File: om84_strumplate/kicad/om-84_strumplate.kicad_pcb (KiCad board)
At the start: 2 copper layers, 117.2 x 151.8 mm, 0 parts

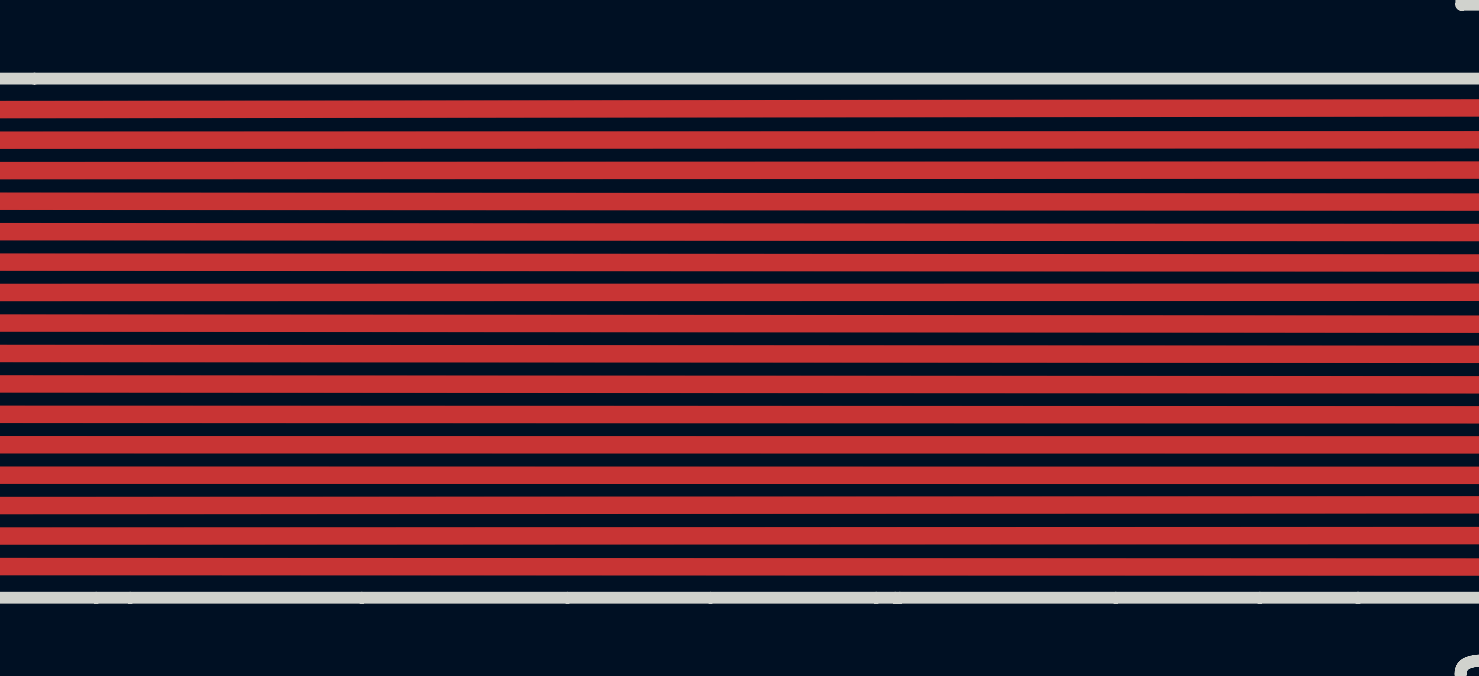
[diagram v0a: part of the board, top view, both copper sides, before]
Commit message: Add Key & Cable Co. branding to both flex tails
White silkscreen on the ribbon tail of the OM-84 and OM-27 flex PCBs:
the piano-key mark (10 mm, white key outlined, black key and plug
filled, cable as a 0.25 mm stroke), "Key & Cable Co." and
"keyandcable.com" in stroke text, and a QR code for
https://keyandcable.com. The QR is version 3 at ECC level H; the ink
prints the light modules and a 3-module quiet zone so the amber
coverlay forms the dark modules. OM-84 uses 0.45 mm modules, the
narrower OM-27 tail uses 0.42 mm. Everything sits over the traces,
clear of the contacts, mask openings and gold-finger stiffeners.

The artwork lives in lib/keyandcable_branding.pretty as reusable
footprints, with a project fp-lib-table in each KiCad folder.
F_Silkscreen gerbers re-plotted with the stored board plot settings
and the production zips updated.

Co-Authored-By: Claude Fable 5.1 <noreply@anthropic.com>
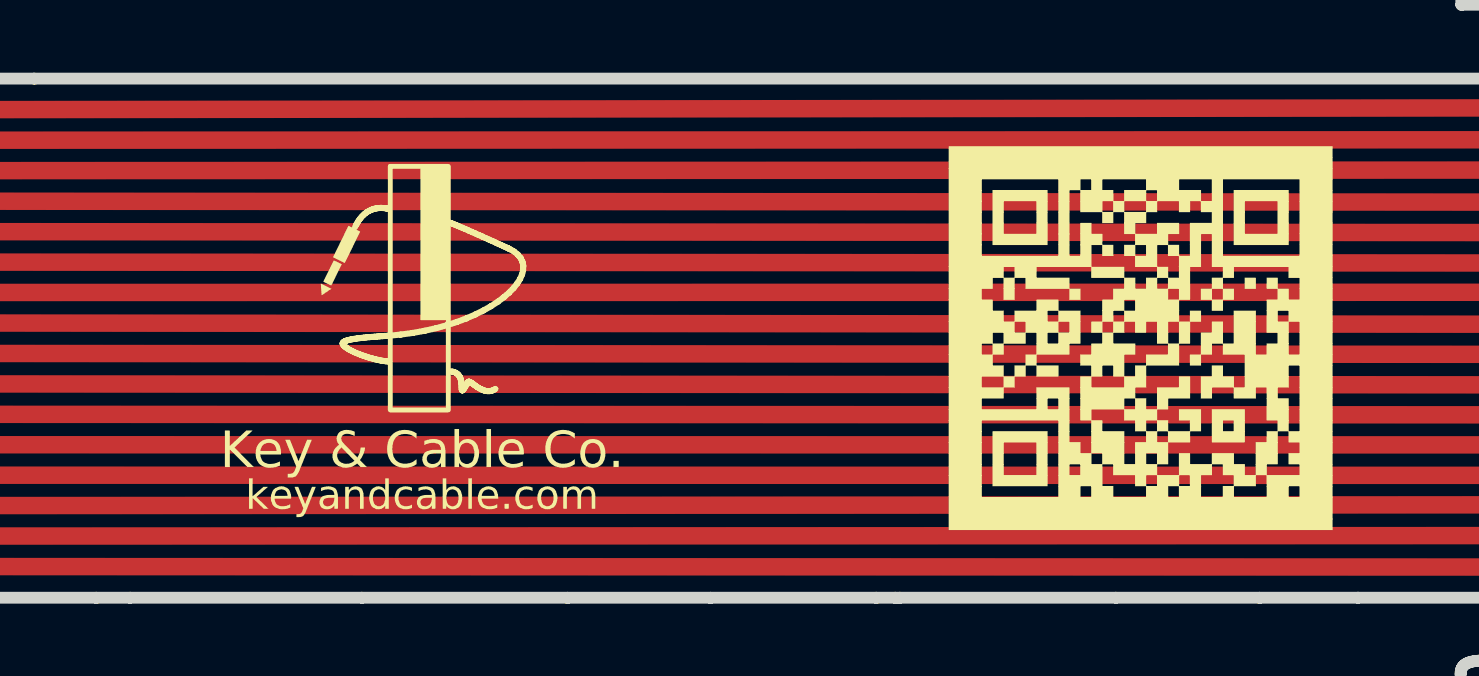
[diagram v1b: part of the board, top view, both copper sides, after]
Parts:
- added REF**: KeyAndCable_Logo, keyandcable_branding:KeyAndCable_Logo, F.Cu at (104.0, 146.6)
- added REF**: KeyAndCable_QR_45, keyandcable_branding:KeyAndCable_QR_45, F.Cu at (133.5, 146.6)

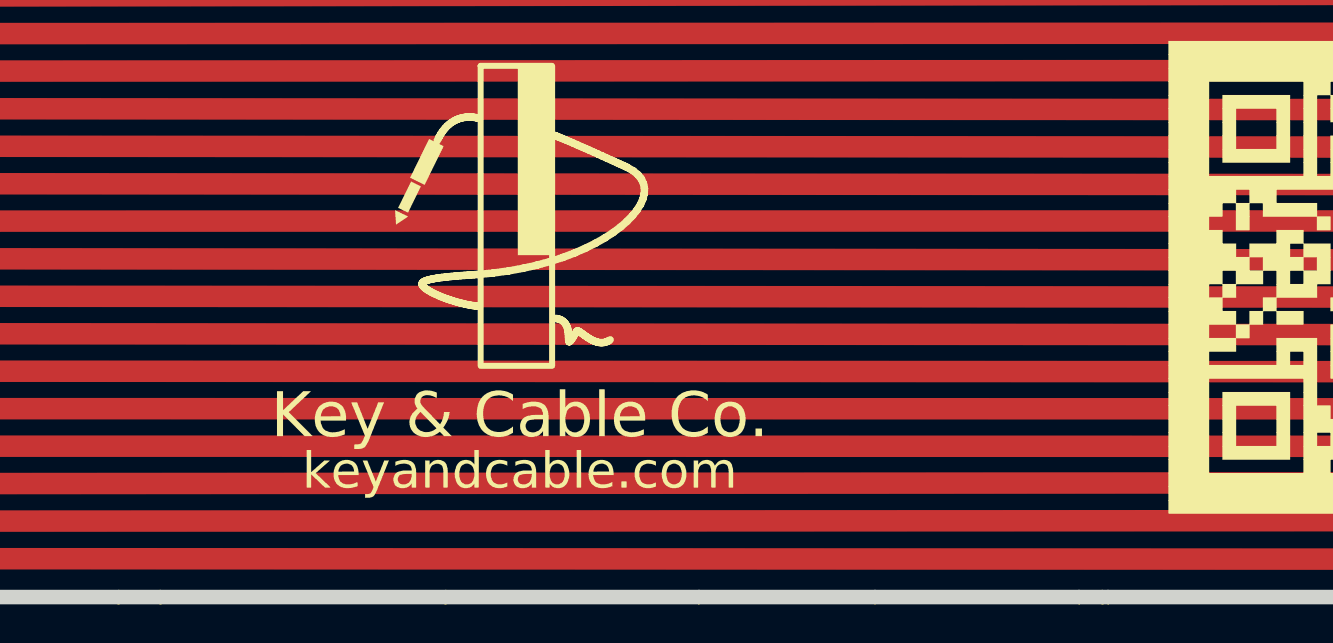
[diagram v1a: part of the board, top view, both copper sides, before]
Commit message: Label both flex tails with model and version V1.1
Each tail now carries its model in bold 2 mm silkscreen ("OM-84" /
"OM-27") with the version under it. The version is printed from the
board's title-block revision via ${REVISION}, so it is bumped in
Board Setup > Title Block and also lands in the Gerber X2 headers.
Both boards are set to 1.1: V1.0 was the first fab run, V1.1 adds the
1.25 mm finger pitch fix and the Key & Cable branding.

On the OM-84 the labels sit horizontally between the logo and the QR.
The OM-27 tail has about 40 mm between the bend and the stiffener, so
its labels are rotated 90 degrees into a column, and the logo and QR
are re-spaced to keep at least 1.3 mm between elements and 1.3 mm
from the stiffener. The company name in the logo lockup drops from
1.5 mm to 1.3 mm text to make room.

F_Silkscreen gerbers re-plotted and the production zips updated.

Co-Authored-By: Claude Opus 5.5 <noreply@anthropic.com>
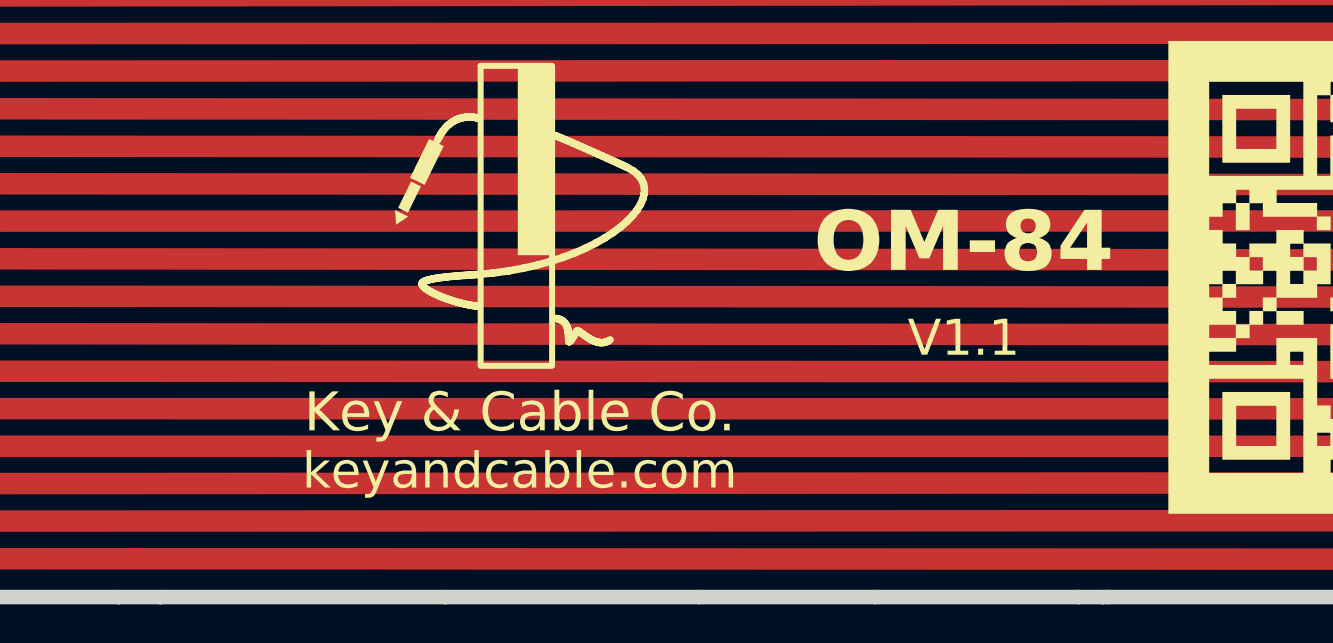
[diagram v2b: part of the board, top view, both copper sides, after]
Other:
- board text added: "OM-84"
- board text added: "V${REVISION}"
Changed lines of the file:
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@@
 	)
 	(paper "A4")
+	(title_block
+		(title "OM-84 Strumplate Flex PCB")
+		(date "2026-10-08")
+		(rev "1.1")
+		(company "Key & Cable Co.")
+	)
 	(layers
 		(0 "F.Cu" signal)
@@
 		)
 		(fp_text user "Key & Cable Co."
-			(at 0 4.6 0)
+			(at 0 4.5 0)
 			(layer "F.SilkS")
 			(effects
 				(font
-					(size 1.5 1.5)
-					(thickness 0.18)
+					(size 1.3 1.3)
+					(thickness 0.16)
 				)
 			)
@@
 		(embedded_fonts no)
 	)
+	(gr_text "OM-84"
+		(at 118.8 145.4 0)
+		(layer "F.SilkS")
+		(effects
+			(font
+				(size 2 2)
+				(thickness 0.3)
+				(bold yes)
+			)
+		)
+	)
+	(gr_text "V${REVISION}"
+		(at 118.8 148.6 0)
+		(layer "F.SilkS")
+		(effects
+			(font
+				(size 1.2 1.2)
+				(thickness 0.18)
+			)
+		)
+	)
 	(gr_line
